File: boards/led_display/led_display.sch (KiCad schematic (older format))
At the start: 54 parts

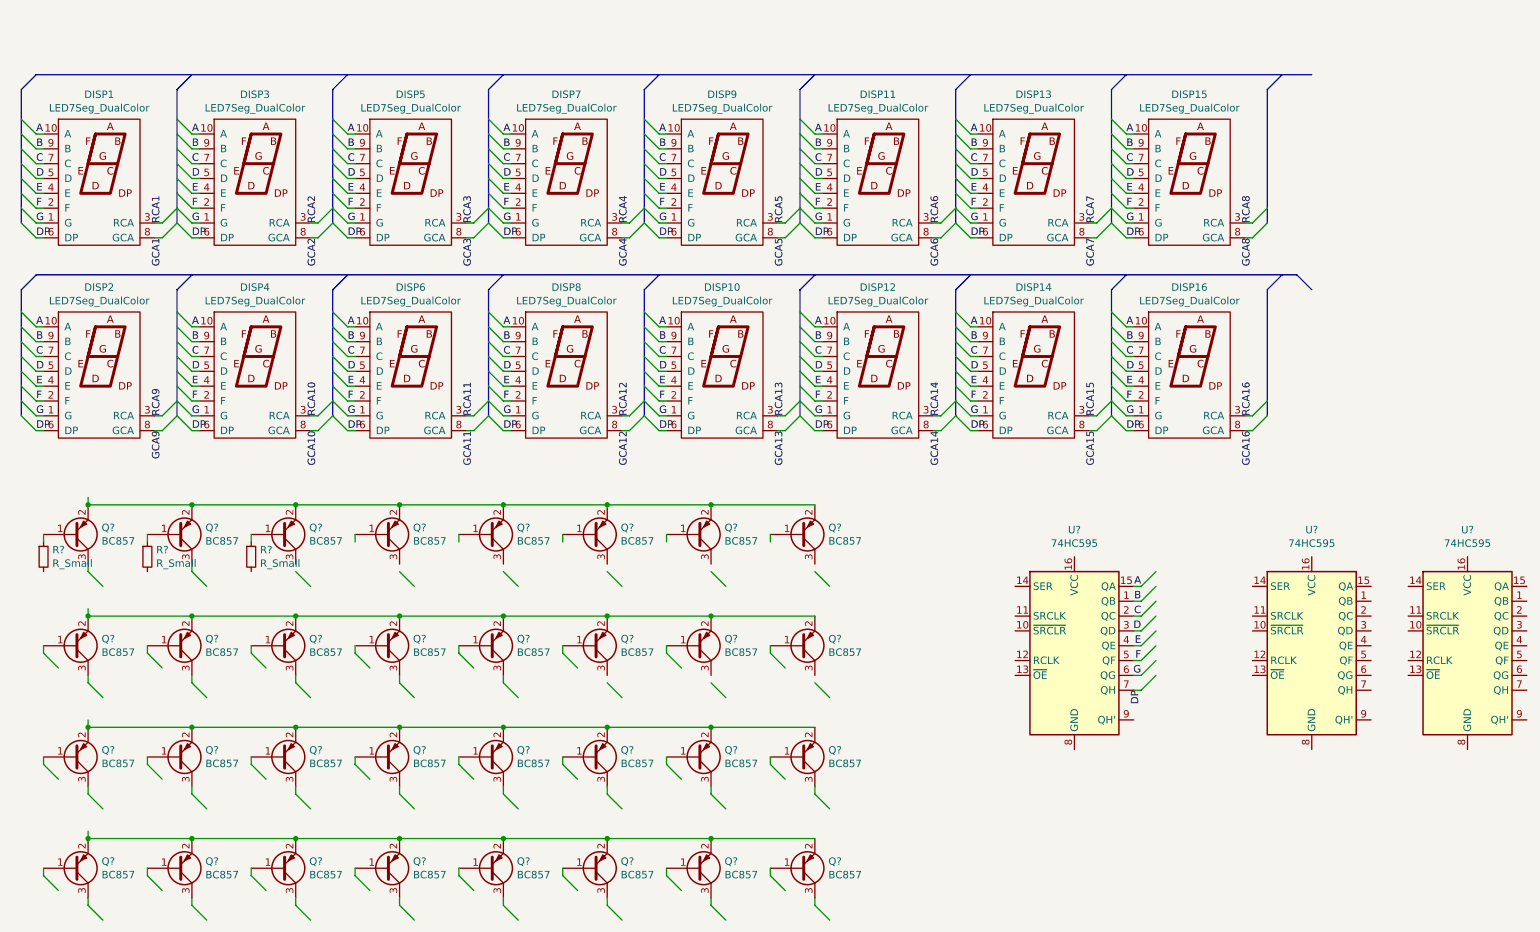
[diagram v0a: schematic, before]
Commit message: Add partial led board layout
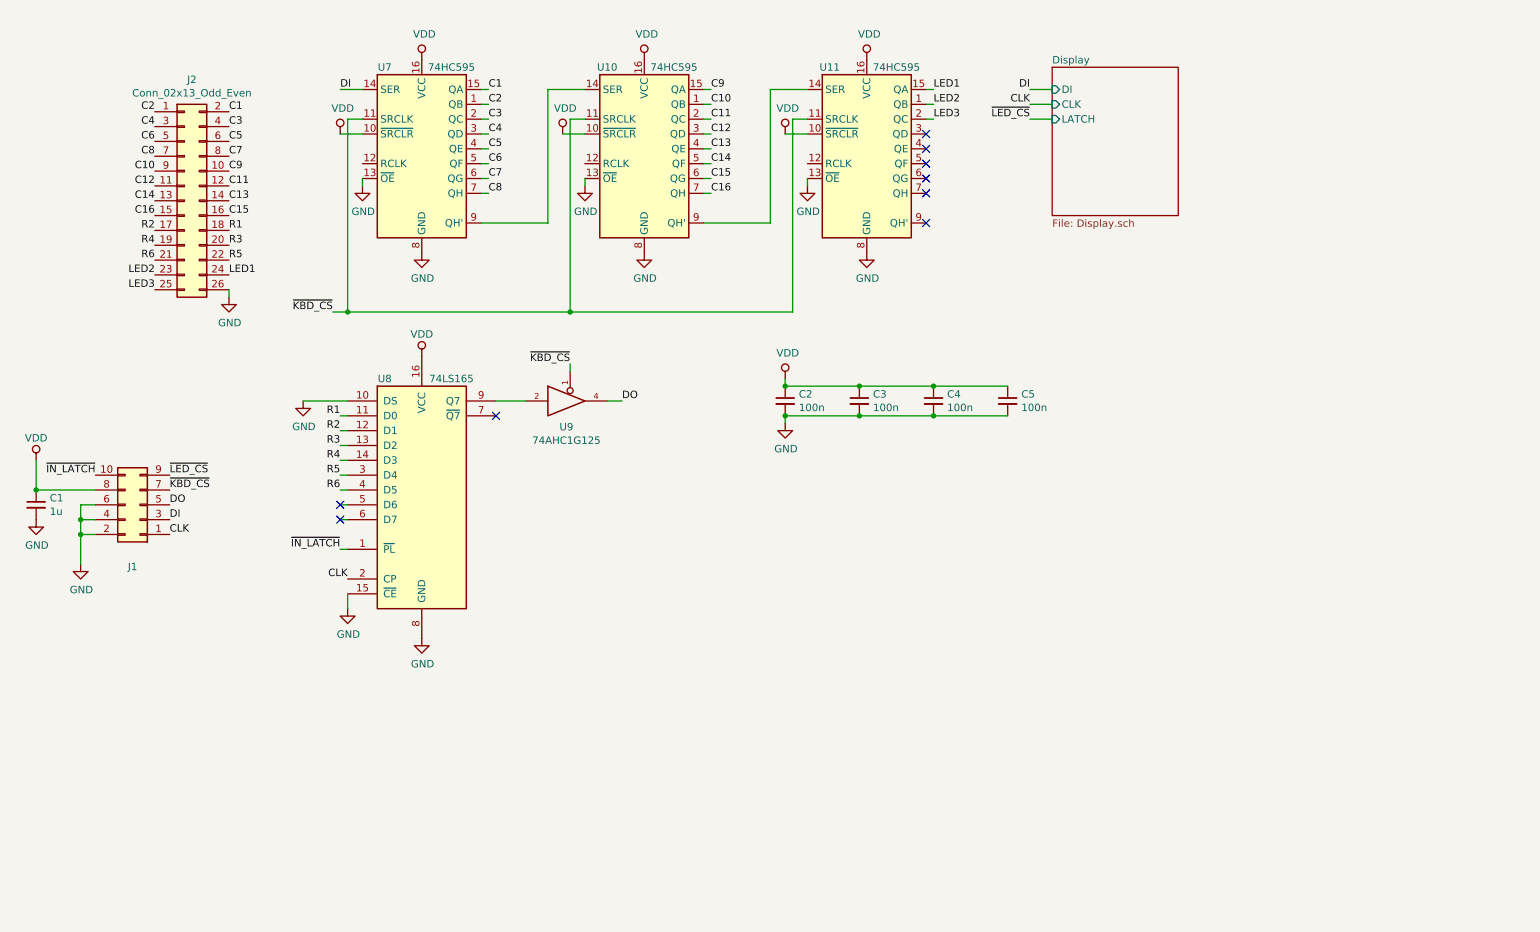
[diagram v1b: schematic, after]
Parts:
- removed DISP1, DISP10, DISP11, DISP12, DISP13, DISP14, DISP15, DISP16, DISP2, DISP3, DISP4, DISP5, DISP6, DISP7, DISP8, DISP9: LED7Seg_DualColor, led_display:LED7Seg_Vertical_039inch, symbol led_display:LED7Seg_DualColor
- removed Q? (x32): BC857, Package_TO_SOT_SMD:SOT-23, symbol Transistor_BJT:BC857
- removed R? (x3): R_Small, symbol Device:R_Small
- removed U? (x3): 74HC595, symbol 74xx:74HC595
- added C1: 1u, Capacitor_SMD:C_0805_2012Metric, symbol Device:C_Small
- added C2, C3, C4, C5: 100n, Capacitor_SMD:C_0603_1608Metric, symbol Device:C_Small
- added J1: Conn_02x05_Odd_Even, Connector_IDC:IDC-Header_2x05_P2.54mm_Vertical, symbol Connector_Generic:Conn_02x05_Odd_Even
- added J2: Conn_02x13_Odd_Even, Connector_IDC:IDC-Header_2x13_P2.54mm_Vertical, symbol Connector_Generic:Conn_02x13_Odd_Even
- added U10, U11, U7: 74HC595, Package_SO:SOIC-16_3.9x9.9mm_P1.27mm, symbol 74xx:74HC595
- added U8: 74LS165, Package_SO:SOIC-16_3.9x9.9mm_P1.27mm, symbol 74xx:74LS165
- added U9: 74AHC1G125, Package_TO_SOT_SMD:SOT-23-5, symbol 74xGxx:74AHC1G125
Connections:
- new net: U10.14 (SER), U7.9 (QH')
- new net: U10.9 (QH'), U11.14 (SER)
- new net: U8.9 (Q7), U9.2
- new net C1: J2.2 (Pin_2), U7.15 (QA)
- new net C10: J2.9 (Pin_9), U10.1 (QB)
- new net C11: J2.12 (Pin_12), U10.2 (QC)
- new net C12: J2.11 (Pin_11), U10.3 (QD)
- new net C13: J2.14 (Pin_14), U10.4 (QE)
- new net C14: J2.13 (Pin_13), U10.5 (QF)
- new net C15: J2.16 (Pin_16), U10.6 (QG)
- new net C16: J2.15 (Pin_15), U10.7 (QH)
- new net C2: J2.1 (Pin_1), U7.1 (QB)
- new net C3: J2.4 (Pin_4), U7.2 (QC)
- new net C4: J2.3 (Pin_3), U7.3 (QD)
- new net C5: J2.6 (Pin_6), U7.4 (QE)
- new net C6: J2.5 (Pin_5), U7.5 (QF)
- new net C7: J2.8 (Pin_8), U7.6 (QG)
- new net C8: J2.7 (Pin_7), U7.7 (QH)
- new net C9: J2.10 (Pin_10), U10.15 (QA)
- new net CLK: J1.1 (Pin_1), U8.2 (CP)
- new net DI: J1.3 (Pin_3), U7.14 (SER)
- new net DO: J1.5 (Pin_5), U9.4
- new net GND: C1.2, C2.2, C3.2, C4.2, C5.2, J1.2 (Pin_2), J1.4 (Pin_4), J1.6 (Pin_6), J2.26 (Pin_26), U10.13 (~OE), U10.8 (GND), U11.13 (~OE), U11.8 (GND), U7.13 (~OE), U7.8 (GND), U8.10 (DS), U8.15 (~CE), U8.8 (GND), U9.3 (GND)
- new net LED1: J2.24 (Pin_24), U11.15 (QA)
- new net LED2: J2.23 (Pin_23), U11.1 (QB)
- new net LED3: J2.25 (Pin_25), U11.2 (QC)
- new net R1: J2.18 (Pin_18), U8.11 (D0)
- new net R2: J2.17 (Pin_17), U8.12 (D1)
- new net R3: J2.20 (Pin_20), U8.13 (D2)
- new net R4: J2.19 (Pin_19), U8.14 (D3)
- new net R5: J2.22 (Pin_22), U8.3 (D4)
- new net R6: J2.21 (Pin_21), U8.4 (D5)
- new net VCC: U9.5 (VCC)
- new net VDD: C1.1, C2.1, C3.1, C4.1, C5.1, J1.8 (Pin_8), U10.10 (~SRCLR), U10.16 (VCC), U11.10 (~SRCLR), U11.16 (VCC), U7.10 (~SRCLR), U7.16 (VCC), U8.16 (VCC)
- new net ~IN_LATCH: J1.10 (Pin_10), U8.1 (~PL)
- new net ~KBD_CS: J1.7 (Pin_7), U10.11 (SRCLK), U11.11 (SRCLK), U7.11 (SRCLK), U9.1
- new net ~LED_CS: J1.9 (Pin_9)
- no-connect marks 0 -> 9

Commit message: Update schematics
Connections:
- net CLK: now also J1.2 (Pin_2), U10.11 (SRCLK), U11.11 (SRCLK), U7.11 (SRCLK); no longer J1.1 (Pin_1)
- net DI: now also J1.4 (Pin_4); no longer J1.3 (Pin_3)
- net DO: now also J1.6 (Pin_6); no longer J1.5 (Pin_5)
- net GND: now also J1.1 (Pin_1), J1.3 (Pin_3), J1.5 (Pin_5); no longer J1.2 (Pin_2), J1.4 (Pin_4), J1.6 (Pin_6)
- net LED1: now also U11.1 (QB); no longer U11.15 (QA)
- net LED2: now also U11.2 (QC); no longer U11.1 (QB)
- net LED3: now also U11.3 (QD); no longer U11.2 (QC)
- net R1: now also U8.6 (D7); no longer U8.11 (D0)
- net R2: now also U8.11 (D0); no longer U8.12 (D1)
- net R3: now also U8.5 (D6); no longer U8.13 (D2)
- net R4: now also U8.12 (D1); no longer U8.14 (D3)
- net R5: now also U8.4 (D5); no longer U8.3 (D4)
- net R6: now also U8.13 (D2); no longer U8.4 (D5)
- net VCC: now also C1.1, C2.1, C3.1, C4.1, C5.1, J1.7 (Pin_7), U10.10 (~SRCLR), U10.16 (VCC), U11.10 (~SRCLR), U11.16 (VCC), U7.10 (~SRCLR), U7.16 (VCC), U8.16 (VCC)
- net ~IN_LATCH: now also J1.9 (Pin_9); no longer J1.10 (Pin_10)
- net ~KBD_CS: now also J1.8 (Pin_8), U10.12 (RCLK), U11.12 (RCLK), U7.12 (RCLK); no longer J1.7 (Pin_7), U10.11 (SRCLK), U11.11 (SRCLK), U7.11 (SRCLK)
- net ~LED_CS: now also J1.10 (Pin_10); no longer J1.9 (Pin_9)
- removed net VDD: C1.1, C2.1, C3.1, C4.1, C5.1, J1.8 (Pin_8), U10.10 (~SRCLR), U10.16 (VCC), U11.10 (~SRCLR), U11.16 (VCC), U7.10 (~SRCLR), U7.16 (VCC), U8.16 (VCC)
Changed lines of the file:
@@
-$EndComp
-$Comp
-L Connector_Generic:Conn_02x05_Odd_Even J1
-U 1 1 6212AA7C
-P 1650 3800
-F 0 "J1" H 1700 4217 50  0000 C CNN
-F 1 "Conn_02x05_Odd_Even" H 1700 4126 50  0001 C CNN
-F 2 "Connector_IDC:IDC-Header_2x05_P2.54mm_Vertical" H 1650 3800 50  0001 C CNN
-F 3 "~" H 1650 3800 50  0001 C CNN
-	1    1650 3800
-	-1   0    0    1
 $EndComp
 $Comp
@@
 $EndComp
 $Comp
-L power:VDD #PWR0127
-U 1 1 621720AA
-P 3550 800
-F 0 "#PWR0127" H 3550 650 50  0001 C CNN
-F 1 "VDD" H 3567 973 50  0000 C CNN
-F 2 "" H 3550 800 50  0001 C CNN
-F 3 "" H 3550 800 50  0001 C CNN
-	1    3550 800
-	1    0    0    -1
-$EndComp
-$Comp
 L power:VDD #PWR0128
 U 1 1 62172826
-P 5050 800
-F 0 "#PWR0128" H 5050 650 50  0001 C CNN
-F 1 "VDD" H 5067 973 50  0000 C CNN
-F 2 "" H 5050 800 50  0001 C CNN
-F 3 "" H 5050 800 50  0001 C CNN
-	1    5050 800
+P 5050 700
+F 0 "#PWR0128" H 5050 550 50  0001 C CNN
+F 1 "VDD" H 5067 873 50  0000 C CNN
+F 2 "" H 5050 700 50  0001 C CNN
+F 3 "" H 5050 700 50  0001 C CNN
+	1    5050 700
 	1    0    0    -1
 $EndComp
@@
 L power:VDD #PWR0129
 U 1 1 6217309D
-P 6550 800
-F 0 "#PWR0129" H 6550 650 50  0001 C CNN
-F 1 "VDD" H 6567 973 50  0000 C CNN
-F 2 "" H 6550 800 50  0001 C CNN
-F 3 "" H 6550 800 50  0001 C CNN
-	1    6550 800
+P 6550 700
+F 0 "#PWR0129" H 6550 550 50  0001 C CNN
+F 1 "VDD" H 6567 873 50  0000 C CNN
+F 2 "" H 6550 700 50  0001 C CNN
+F 3 "" H 6550 700 50  0001 C CNN
+	1    6550 700
 	1    0    0    -1
 $EndComp
@@
 	5450 1700 5500 1700
 Wire Wire Line
-	6950 1000 7000 1000
-Wire Wire Line
 	6950 1100 7000 1100
 Wire Wire Line
 	6950 1200 7000 1200
+Wire Wire Line
+	6950 1300 7000 1300
 Text Label 4000 1000 0    50   ~ 0
 C1
@@
 Text Label 5500 1700 0    50   ~ 0
 C16
-Text Label 7000 1000 0    50   ~ 0
+Text Label 7000 1100 0    50   ~ 0
 LED1
-Text Label 7000 1100 0    50   ~ 0
+Text Label 7000 1200 0    50   ~ 0
 LED2
-Text Label 7000 1200 0    50   ~ 0
+Text Label 7000 1300 0    50   ~ 0
 LED3
 Wire Wire Line
@@
 Wire Wire Line
 	3050 3900 3000 3900
+Text Label 3000 3900 2    50   ~ 0
+R1
 Text Label 3000 3200 2    50   ~ 0
-R1
+R2
+Text Label 3000 3800 2    50   ~ 0
+R3
 Text Label 3000 3300 2    50   ~ 0
-R2
+R4
+Text Label 3000 3700 2    50   ~ 0
+R5
 Text Label 3000 3400 2    50   ~ 0
-R3
-Text Label 3000 3500 2    50   ~ 0
-R4
-Text Label 3000 3600 2    50   ~ 0
-R5
-Text Label 3000 3700 2    50   ~ 0
 R6
 $Comp
@@
 Text Label 1750 2350 2    50   ~ 0
 LED3
-NoConn ~ 6950 1300
 NoConn ~ 6950 1400
 NoConn ~ 6950 1500
 NoConn ~ 6950 1600
 NoConn ~ 6950 1700
-Wire Wire Line
-	3150 1200 3050 1200
-Wire Wire Line
-	3050 1200 3050 2500
-Wire Wire Line
-	4650 1200 4550 1200
-Wire Wire Line
-	4550 1200 4550 2500
-Wire Wire Line
-	6150 1200 6050 1200
-Wire Wire Line
-	6050 1200 6050 2500
 Wire Wire Line
 	3050 2500 4550 2500
@@
 	1    0    0    -1
 $EndComp
-NoConn ~ 3000 3800
-NoConn ~ 3000 3900
 $Comp
 L power:GND #PWR0138
@@
 Connection ~ 6500 3000
 Wire Wire Line
-	6500 3000 6000 3000
+	6500 3000 6200 3000
 Connection ~ 7000 3000
 Wire Wire Line
@@
 	1    0    0    -1
 $EndComp
+NoConn ~ 3000 3500
+NoConn ~ 3000 3600
+$Comp
+L Connector_Generic:Conn_02x05_Odd_Even J1
+U 1 1 6212AA7C
+P 1550 3800
+F 0 "J1" H 1600 4100 50  0000 C CNN
+F 1 "Conn_02x05_Odd_Even" H 1600 4126 50  0001 C CNN
+F 2 "Connector_IDC:IDC-Header_2x05_P2.54mm_Vertical" H 1550 3800 50  0001 C CNN
+F 3 "~" H 1550 3800 50  0001 C CNN
+	1    1550 3800
+	1    0    0    1
+$EndComp
+$Comp
+L power:VCC #PWR0154
+U 1 1 6228EB46
+P 6200 2950
+F 0 "#PWR0154" H 6200 2800 50  0001 C CNN
+F 1 "VCC" H 6217 3123 50  0000 C CNN
+F 2 "" H 6200 2950 50  0001 C CNN
+F 3 "" H 6200 2950 50  0001 C CNN
+	1    6200 2950
+	1    0    0    -1
+$EndComp
+Wire Wire Line
+	6200 2950 6200 3000
+Connection ~ 6200 3000
+Wire Wire Line
+	6200 3000 6000 3000
+NoConn ~ 6950 1000
+Wire Wire Line
+	3150 1500 3050 1500
+Wire Wire Line
+	3050 1500 3050 2500
+Wire Wire Line
+	4650 1500 4550 1500
+Wire Wire Line
+	4550 1500 4550 2500
+Wire Wire Line
+	6150 1500 6050 1500
+Wire Wire Line
+	6050 1500 6050 2500
+$Comp
+L power:VDD #PWR0127
+U 1 1 621720AA
+P 3550 700
+F 0 "#PWR0127" H 3550 550 50  0001 C CNN
+F 1 "VDD" H 3567 873 50  0000 C CNN
+F 2 "" H 3550 700 50  0001 C CNN
+F 3 "" H 3550 700 50  0001 C CNN
+	1    3550 700
+	1    0    0    -1
+$EndComp
+Wire Wire Line
+	3550 700  3550 800
+Wire Wire Line
+	6550 700  6550 800
+Wire Wire Line
+	5050 700  5050 800
+Wire Wire Line
+	6100 750  6100 1200
+Wire Wire Line
+	6100 1200 6150 1200
+Wire Wire Line
+	4650 1200 4600 1200
+Wire Wire Line
+	4600 1200 4600 750
+Connection ~ 4600 750
+Wire Wire Line
+	4600 750  6100 750
+Wire Wire Line
+	3150 1200 3100 1200
+Wire Wire Line
+	3100 1200 3100 750
+Wire Wire Line
+	3100 750  4600 750
+Wire Wire Line
+	3100 750  3050 750
+Connection ~ 3100 750
+Text Label 3050 750  2    50   ~ 0
+CLK
 $EndSCHEMATC
